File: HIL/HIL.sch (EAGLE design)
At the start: 267 parts, among them J1 JTAG_ARM_10PIN, J4 JTAG_ARM_10PIN, M0S0 TPB1,27, M0S1 TPB1,27, M0S2 TPB1,27, M0S3 TPB1,27, M1S0 M0S3, M1S1 M0S3, M1S2 M0S3, M1S3 M0S3, M2S0 M0S3, M2S1 M0S3, M2S2 M0S3, M2S3 M0S3, U1 CD74HC4067SM96, U10 INA219AIDCNR, U11 INA219AIDCNR, U12 INA219AIDCNR, U13 TM4C1294NCPDT, U14 ADUM1201ARZ, U15 SN65HVD230D, U16 TL1963AKTTR., U17 FT230XS, U2 TL1963AKTTR., U3 CD74HC4067SM96, U4 CD74HC4067SM96, U5 MCP4725A0T-E/CH, U6 TL1963AKTTR., U7 MCP2003-E/SN, U9 INA219AIDCNR, X1 A1944-50, X2 A1944-50, X4 A1944-50, Y3 NX3225GA

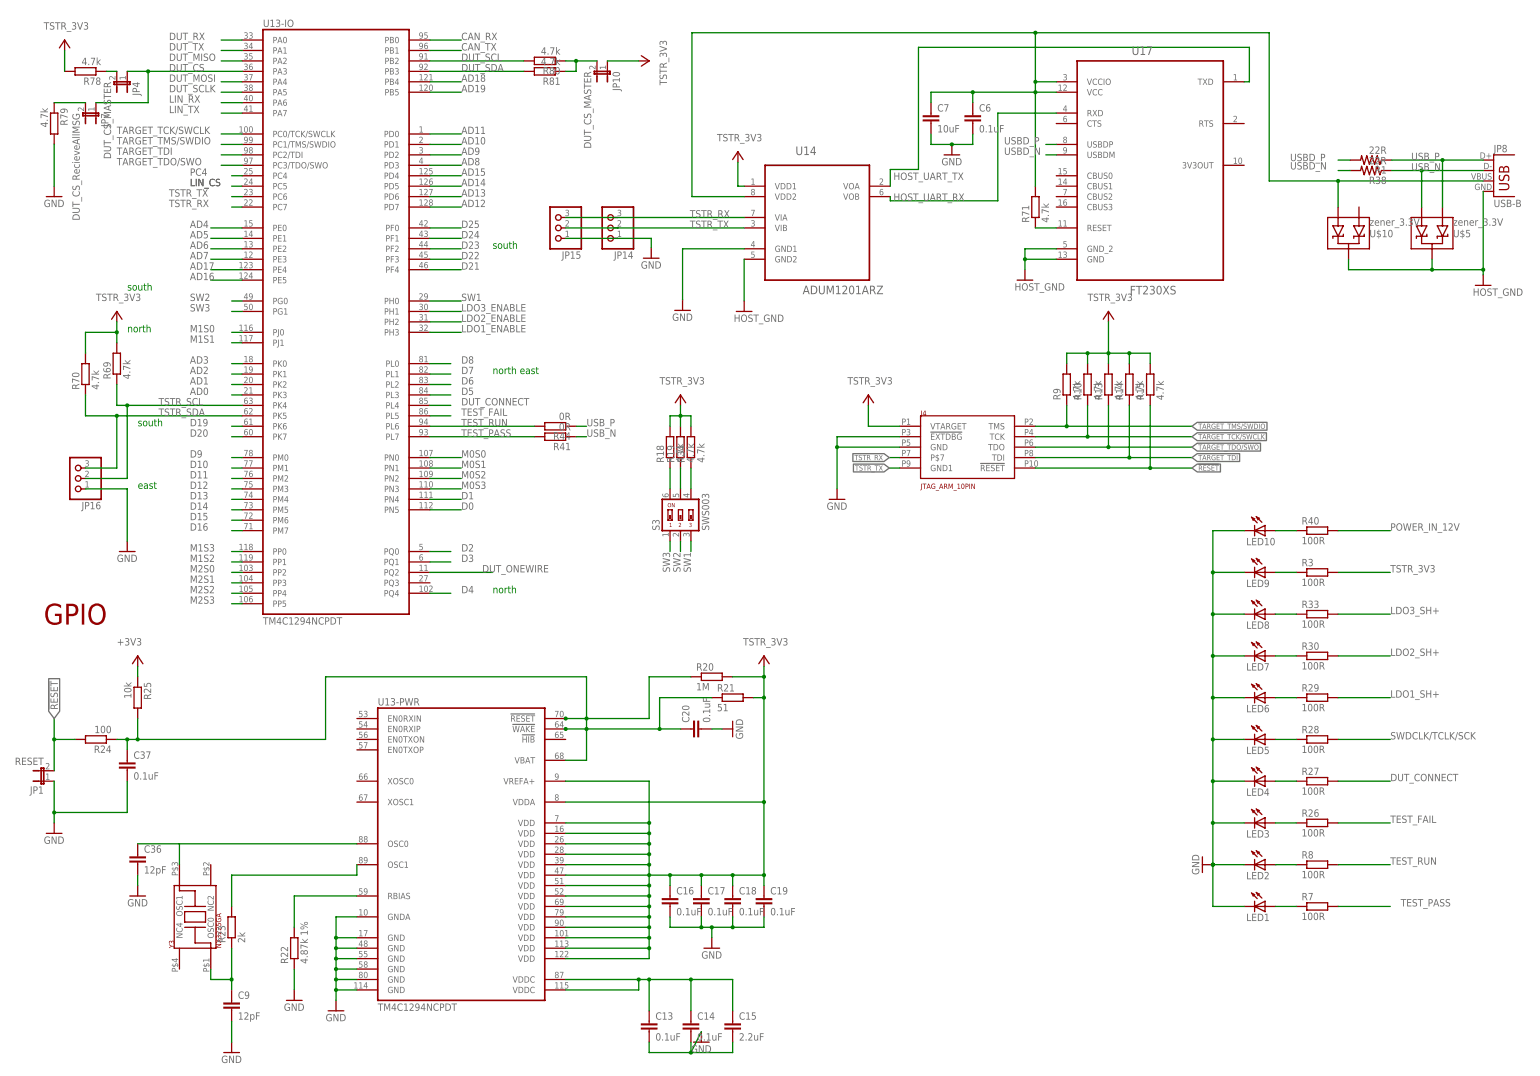
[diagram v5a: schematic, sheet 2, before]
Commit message: Remove: 1 chanel DAC Add: 8 CH DAC Update: libraries
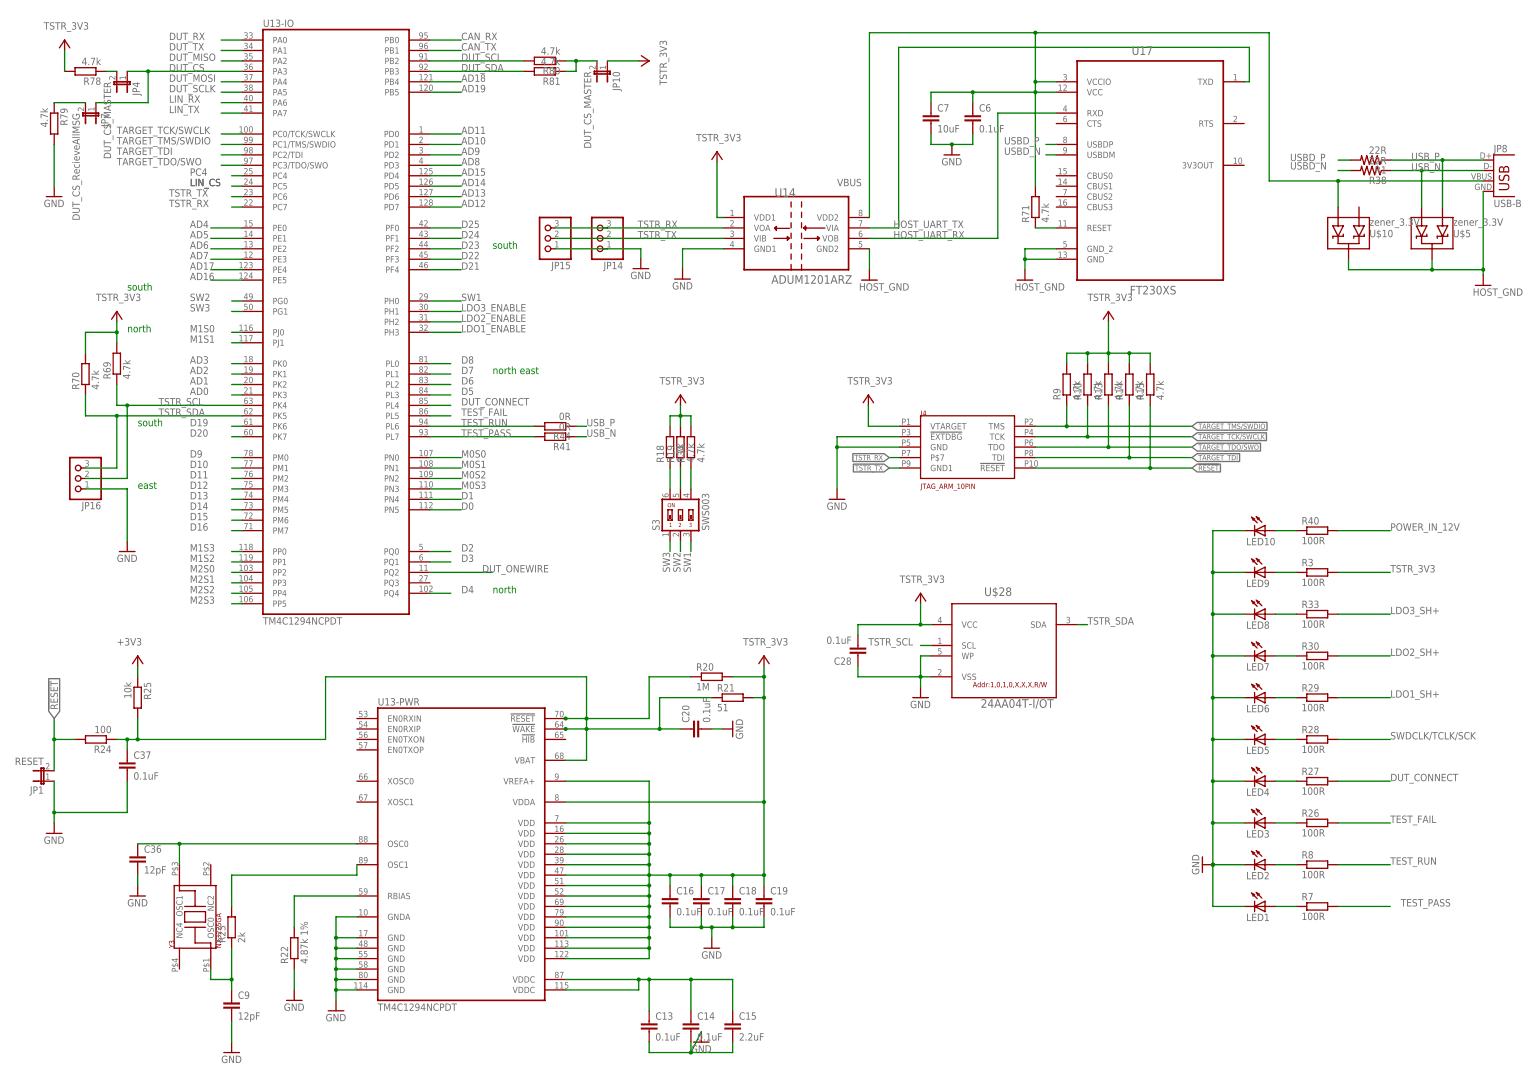
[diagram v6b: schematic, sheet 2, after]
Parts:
- removed U5: MCP4725A0T-E/CH, MCP4725:MCP4725A0T-E/CH
- added C28: 0.1uF, rcl:C-EUC0402K
- added C29: 1uF, rcl:C-EUC0402K
- added C30: 10uF, rcl:C-EUC0402K
- added R89: 4k7, resistor:R-EU_R0402
- added U$28: 24AA04T-I/OT, microchip_E14:24AA04T-I/OT
- added U8: DAC7578SPW, Texas Instruments_E14:DAC7578SPW
- R46: value 4.7k -> 4k7
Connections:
- net ADJ3 renamed LDO1_ADJ
- net ADJ4 renamed LDO2_ADJ
- net ADJ5 renamed LDO3_ADJ
- net N$40 renamed VIN
- removed net N$216: C23.1, U$34.VIN
- new net AOUT_1: U8.VOUTA
- new net AOUT_2: U8.VOUTB
- new net AOUT_3: U8.VOUTC
- new net AOUT_4: U8.VOUTD
- new net AOUT_5: U8.VOUTE
- new net AOUT_6: U8.VOUTF
- new net AOUT_7: U8.VOUTG
- new net AOUT_8: U8.VOUTH
- new net N$40: C29.2, C3.2, C30.2, R46.1, R89.2, U8.AVDD, U8.VREFIN
- new net N$81: R89.1, U8.~CLR
- net DUT_AOUT1: no longer U5.VOUT
- net GND: now also C28.1, C29.1, C3.1, C30.1, U$28.VSS, U$28.WP, U8.GND; no longer C3.2, R46.2, U5.VSS
- net HOST_UART_TX: now also U14.VIA; no longer U14.VOA
- net N$1: now also R46.2, U8.~LDAC; no longer R46.1, U5.A0
- net POWER_IN_12V: now also C23.1, U$34.VIN
- net TSTR_3V3: now also C28.2, U$28.VCC; no longer C3.1, U5.VDD
- net TSTR_RX: now also U14.VOA; no longer U14.VIA
- net TSTR_SCL: now also U$28.SCL, U8.SCL; no longer U5.SCL
- net TSTR_SDA: now also U$28.SDA, U8.SDA; no longer U5.SDA
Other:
- note removed: "GPIO"
- moved on the sheet: C3, JP14, JP15, R46

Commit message: Add: - dac headers          - labels to all the headers
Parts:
- removed S3: SWS003, smd-special:SWS003
- added C31: 0.1uF, rcl:C-EUC0402
- added C32, C33: 0.1uF 20V, rcl:C-EUC0402K
- added JP17: (no value), JDT-1800_smahed:PINHD-2X4
- added R120, R121, R122, R123, R90: 4k7, resistor:R-EU_R0402
- added R124: 4k, resistor:R-EU_R0402
- added R125: 24k, resistor:R-EU_R0402
- added R126: 10k, resistor:R-EU_R0402
- added R127: 33k NTC, SparkFun-Passives:RESISTOR1206
- added SJ1, SJ2, SJ3: SOLDERJUMPERROUND, SparkFun-Retired:SOLDERJUMPERROUND
- added SW1: EC12E_SW, switch-alps:EC12E_SW
- added U$29: 3v3, SparkFun-DiscreteSemi:V-REFERENCESMD
- added U5: MAX11647EUA+T, Maxim_E14:MAX11647EUA+T
- C23: value 1uF -> 1uF 20V
- R34: value 4.7k -> 4k7
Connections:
- removed net N$41: R18.1, S3.6
- removed net N$42: R19.1, S3.5
- removed net N$55: U$11.RH
- removed net N$56: U$11.RW
- removed net N$57: U$11.RL, U$11.V+
- removed net N$67: U$12.RH
- removed net N$68: U$12.RW
- removed net N$69: U$12.RL, U$12.V+
- removed net N$72: U$27.RH
- removed net N$73: U$27.RW
- removed net SW1: S3.3, U13-IO.PH0@29
- removed net SW2: S3.2, U13-IO.PG0@49
- removed net SW3: S3.1, U13-IO.PG1@50
- new net LDO1_RW: SJ1.1, U$11.RW
- new net LDO2_RW: SJ2.1, U$12.RW
- new net LDO3_RW: SJ3.1, U$27.RW
- new net N$82: R19.1, SW1G$1.C
- new net NTC_OUT: R126.1, R127.2, U5.AIN1
- new net ROTARY_A: SW1G$1.A, U13-IO.PG0@49
- new net ROTARY_B: SW1G$1.B, U13-IO.PG1@50
- new net ROTARY_SW: SW1G$2.1, U13-IO.PH0@29
- new net SUPPLY_DIV: R124.1, R125.2, U$29.C, U5.AIN0
- net AOUT_1: now also JP17.1
- net AOUT_2: now also JP17.2
- net AOUT_3: now also JP17.3
- net AOUT_4: now also JP17.4
- net AOUT_5: now also JP17.5
- net AOUT_6: now also JP17.6
- net AOUT_7: now also JP17.7
- net AOUT_8: now also JP17.8
- net GND: now also C31.1, C32.2, C33.1, R120.2, R125.1, R127.1, R90.2, SW1G$3.G, SW1G$4.G, U$11.RL, U$12.RL, U$27.RL, U$29.A, U5.GND
- net LDO1_ADJ: now also SJ1.2
- net LDO1_SH+: now also U$11.RH, U$11.V+
- net LDO2_ADJ: now also SJ2.2
- net LDO2_SH+: now also U$12.RH, U$12.V+
- net LDO3_ADJ: now also SJ3.2
- net N$43: now also R18.1, SW1G$2.2; no longer R34.1, S3.4
- net N$53: now also R120.1
- net N$54: now also R121.1
- net N$63: now also R34.1
- net N$66: now also R90.1
- net N$70: now also R122.1
- net N$71: now also R123.1
- net N$74: now also U$27.RH; no longer U$27.RL
- net POWER_IN_12V: now also C33.2, R124.2
- net TSTR_3V3: now also C31.2, C32.1, R121.2, R122.2, R123.2, R126.2, U5.REF, U5.VDD
- net TSTR_SCL: now also U5.SCL
- net TSTR_SDA: now also U5.SDA
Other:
- moved on the sheet: C11, C12, C2, C21, C22, C23, C24, C25, C26, C27, C4, C8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

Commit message: Add DAC layout
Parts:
- added R128: 100k, resistor:R-EU_R0402
- added SJ4: SOLDERJUMPERROUND, SparkFun-Retired:SOLDERJUMPERROUND
- added U$31: ATP101, MosFet_P:ATP101
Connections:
- removed net DUT_AOUT1: JP3.12, R82.2, U$45.A2
- new net N$41: R128.2, U$31.G
- new net VIN_REV: JP12.P$1, JP5.PWR, SJ4.1, U$31.D
- net AOUT_2: now also U8.VOUTC; no longer U8.VOUTB
- net AOUT_3: now also U8.VOUTE; no longer U8.VOUTC
- net AOUT_4: now also U8.VOUTG; no longer U8.VOUTD
- net AOUT_5: now also U8.VOUTB; no longer U8.VOUTE
- net AOUT_6: now also U8.VOUTD; no longer U8.VOUTF
- net AOUT_7: now also U8.VOUTF; no longer U8.VOUTG
- net GND: now also JP3.12, R128.1
- net VIN: now also SJ4.2, U$31.S; no longer JP12.P$1, JP5.PWR
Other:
- moved on the sheet: C1, C10, C11, C12, C2, C21, C25, C26, C27, C31, C4, C5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
